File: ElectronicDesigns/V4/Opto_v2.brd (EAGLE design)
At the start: 167 x 85.1 mm, 5 parts, among them U1 TLV1117-18IDCYG3

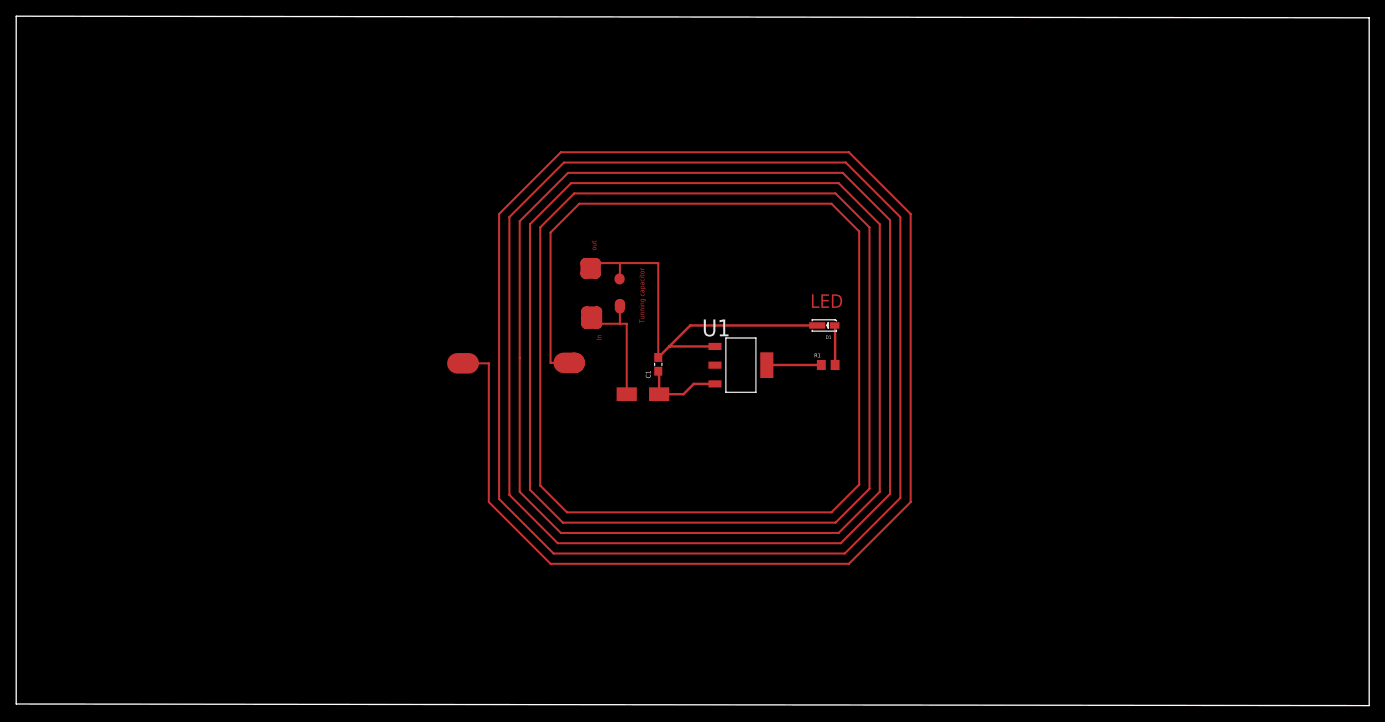
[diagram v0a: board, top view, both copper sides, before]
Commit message: Circuit modified for antenna of Sparkfun
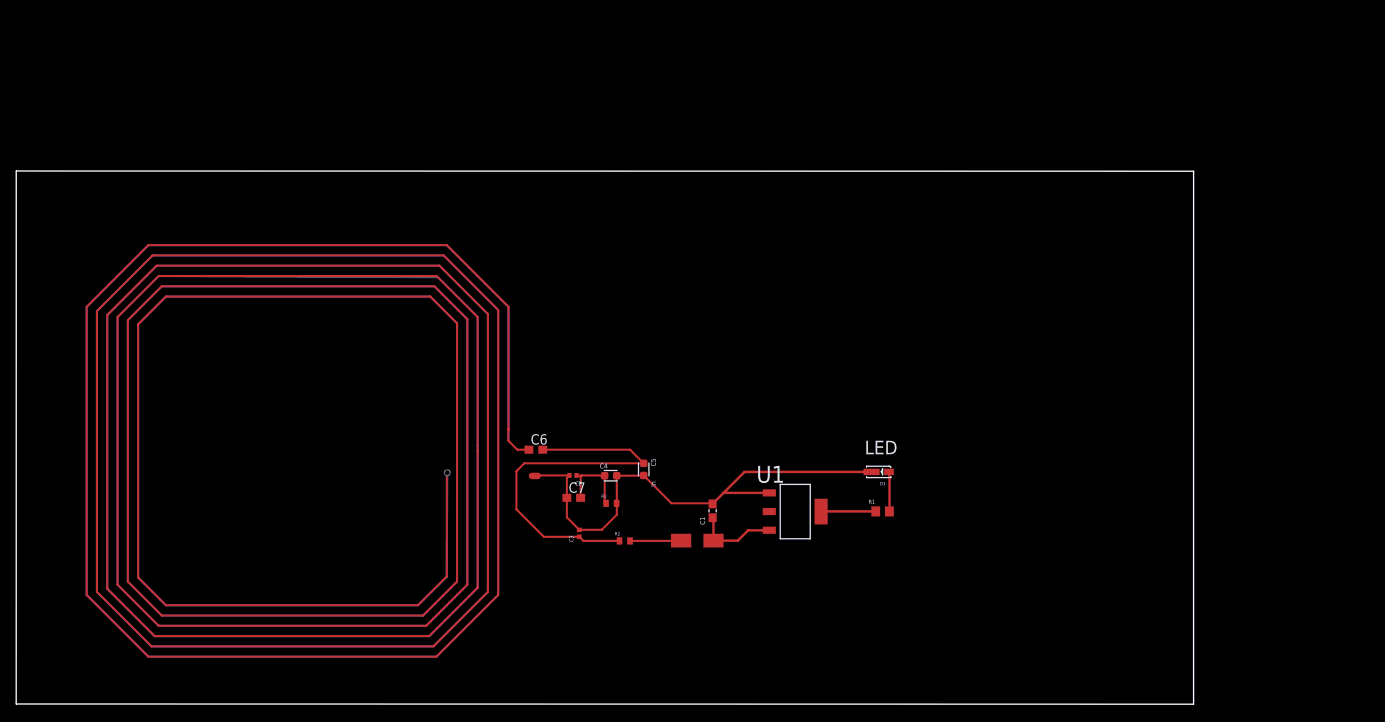
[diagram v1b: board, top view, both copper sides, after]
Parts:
- added C2, C3: 04025A220JAT2A, 04025A220JAT2A:CAPC1005X56N
- added C4, C5: GCM1885C1H270JA16D, GCM1885C1H270JA16D:CAPC1608X9N
- added C6, C7: CC0603JRNPO9BN180, CC0603JRNPO9BN180:0603
- added R2, R3: CRCW04020000Z0EDHP, CRCW04020000Z0EDHP:RESC1005X40
- moved U1 19.3 mm to (80.2, 23.6)
- moved C1 19.3 mm to (70.0, 23.8)
- moved U$1 19.3 mm to (68.1, 20.1)
- moved D1 19.3 mm to (90.5, 28.6)
- moved R1 19.3 mm to (90.9, 23.7)
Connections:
- new net N$3: C2.1, C4.1, C7.2, R3.1
- new net N$5: C3.1, C5.1, C6.2, R2.1
- new net N$6: R2.2, U$1.1
- net GND: now also C2.2, C3.2, C4.2, C5.2, C7.1, R3.2
- net IN+: now also C6.1; no longer U$1.1
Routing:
- net IN+: track 22.2 -> 1071.1 mm
- net GND: track 53.4 -> 980.4 mm, vias 0 -> 1
- net OUT: track 538.5 -> 0.00 mm
- net IN: track 465.6 -> 0.00 mm
- net N$5: track 0.00 -> 48.3 mm
- net N$3: track 0.00 -> 9.93 mm
- net N$6: track 0.00 -> 6.32 mm
- net N$7: track 0.00 -> 0.75 mm
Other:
- board size 167 x 85.1 mm -> 145.3 x 65.8 mm
- board text removed: "Tunning capacitor"
- board text removed: "out"
